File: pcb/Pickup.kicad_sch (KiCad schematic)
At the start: 40 parts, among them IC1 MAX9924UAUB+, Q7 MMBT2222A, T1 SM-LP-5001E, U4 AT223-CuH-S

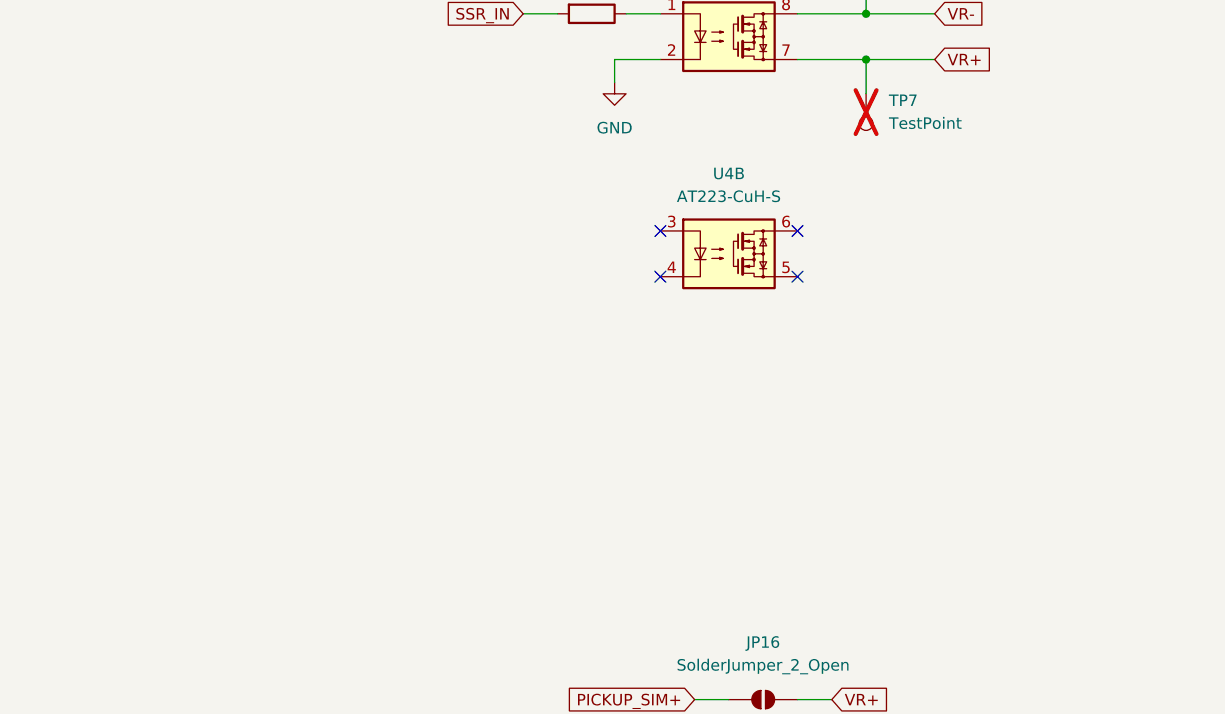
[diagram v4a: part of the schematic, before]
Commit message: added another CDI output sensing (opto coupler)
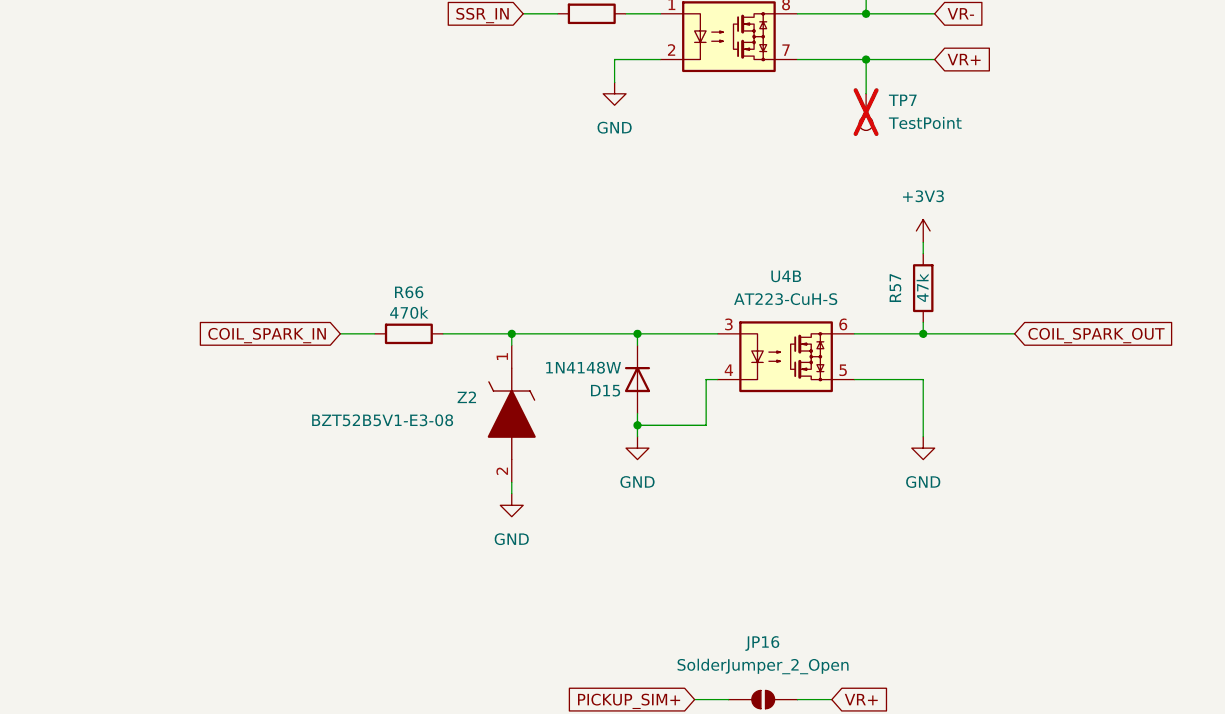
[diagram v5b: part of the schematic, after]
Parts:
- added D15: 1N4148W, Diode_SMD:D_SOD-123, symbol Diode:1N4148W
- added R57: 47k, Resistor_SMD:R_0603_1608Metric, symbol Device:R
- added R66: 470k, Resistor_SMD:R_0603_1608Metric, symbol Device:R
- added Z2: BZT52B5V1-E3-08, SamacSys_Parts:BZT52B5V1E308, symbol SamacSys_Parts:BZT52B5V1-E3-08
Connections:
- net +3V3: now also R57.2
- net GND: now also U4.4, U4.5, D15.2 (A), Z2.2
- net at U4.3: now also D15.1 (K), R66.1, Z2.1
- net COIL_SPARK_OUT: now reaches U4.6
- net COIL_SPARK_OUT: now also R57.1
- new net COIL_SPARK_IN: R66.2
- no-connect marks 6 -> 2
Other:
- moved on the sheet: U4B

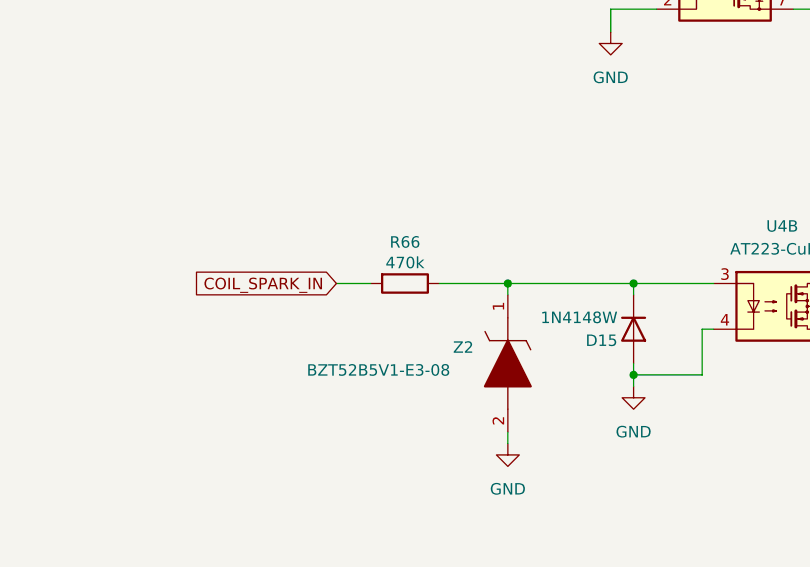
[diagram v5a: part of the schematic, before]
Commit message: changed to THT footprint for better analysis
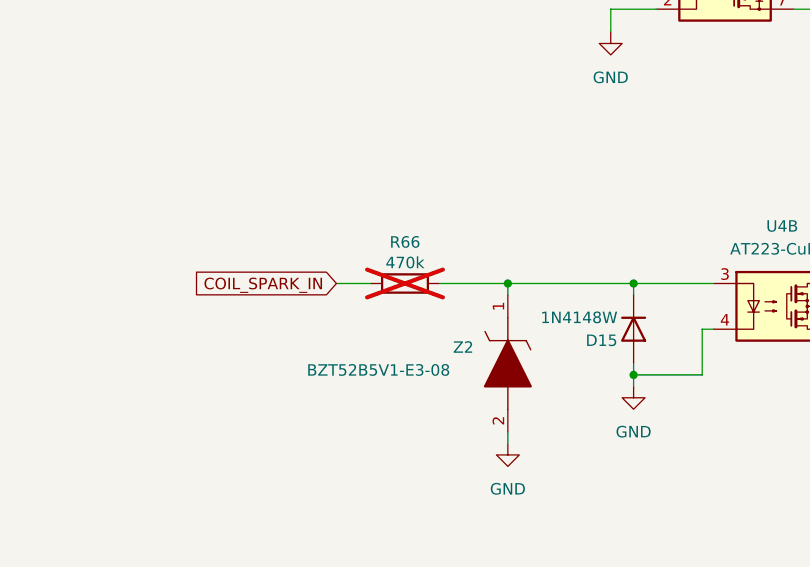
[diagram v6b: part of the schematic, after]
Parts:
- R66: footprint Resistor_SMD:R_0603_1608Metric -> Resistor_THT:R_Axial_DIN0204_L3.6mm_D1.6mm_P1.90mm_Vertical; now not fitted
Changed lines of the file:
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@@
 		(in_bom yes)
 		(on_board yes)
-		(dnp no)
+		(dnp yes)
 		(property "Reference" "R66"
 			(at 194.31 76.708 90)
@@
 			)
 		)
-		(property "Footprint" "Resistor_SMD:R_0603_1608Metric"
+		(property "Footprint" "Resistor_THT:R_Axial_DIN0204_L3.6mm_D1.6mm_P1.90mm_Vertical"
 			(at 194.31 79.502 90)
 			(effects

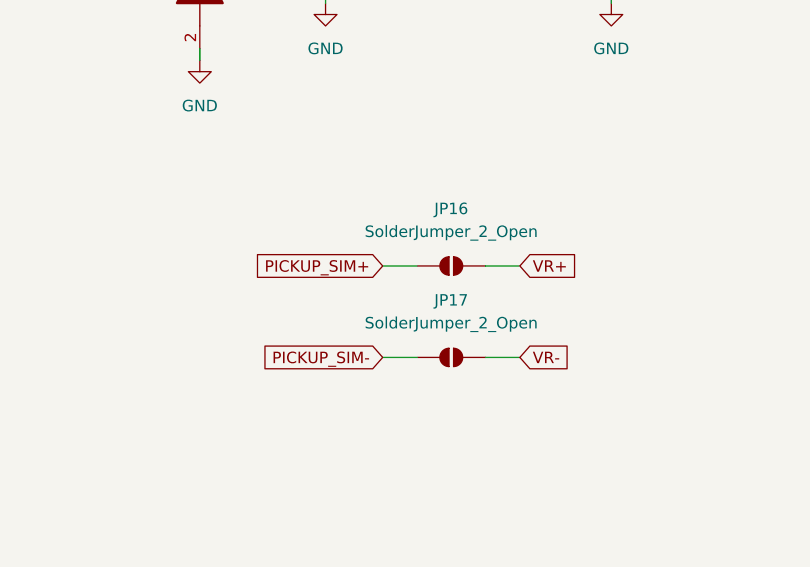
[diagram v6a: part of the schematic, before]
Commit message: removed unnecessary jumpers
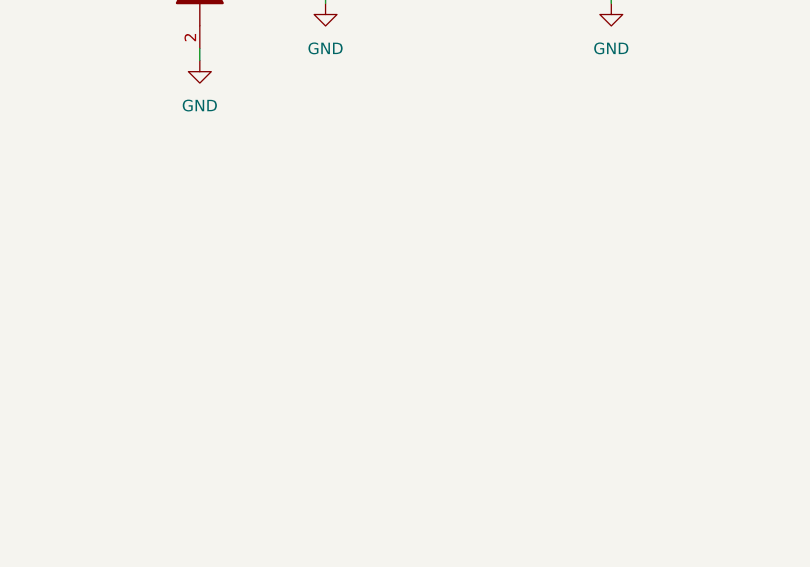
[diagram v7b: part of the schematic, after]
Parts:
- removed JP16, JP17: SolderJumper_2_Open, Jumper:SolderJumper-2_P1.3mm_Open_RoundedPad1.0x1.5mm, symbol Jumper:SolderJumper_2_Open

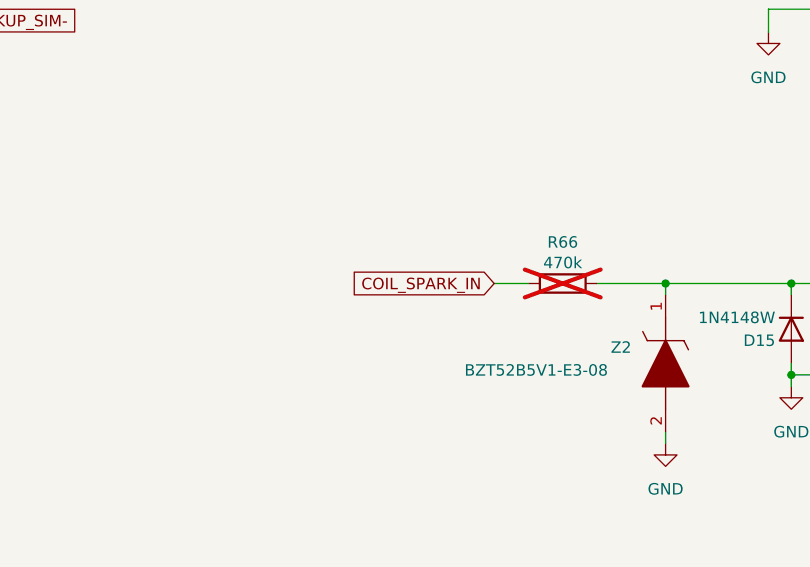
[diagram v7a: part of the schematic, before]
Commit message: MCU labels rework
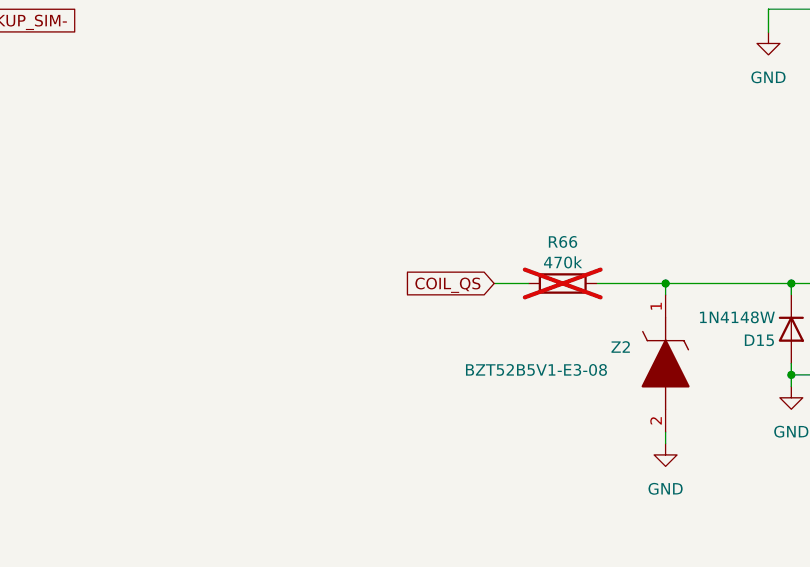
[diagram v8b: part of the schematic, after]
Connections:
- net COIL_SPARK_IN renamed COIL_QS
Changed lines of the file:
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@@
+		)
+	)
+	(global_label "COIL_QS"
+		(shape input)
+		(at 186.69 81.28 180)
+		(fields_autoplaced yes)
+		(effects
+			(font
+				(size 1.27 1.27)
+			)
+			(justify right)
+		)
+		(property "Intersheetrefs" "${INTERSHEET_REFS}"
+			(at 175.9638 81.28 0)
+			(effects
+				(font
+					(size 1.27 1.27)
+				)
+				(justify right)
+				(hide yes)
+			)
 		)
 	)
@@
 			(effects
 				(font
-					(size 1.27 1.27)
-				)
-				(justify right)
-				(hide yes)
-			)
-		)
-	)
-	(global_label "COIL_SPARK_IN"
-		(shape input)
-		(at 186.69 81.28 180)
-		(fields_autoplaced yes)
-		(effects
-			(font
-				(size 1.27 1.27)
-			)
-			(justify right)
-		)
-		(property "Intersheetrefs" "${INTERSHEET_REFS}"
-			(at 169.4928 81.28 0)
-			(effects
-				(font
